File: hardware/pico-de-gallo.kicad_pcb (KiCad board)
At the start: 4 copper layers, 50 x 69.5 mm, 14 parts, among them J1 Conn_02x08_Odd_Even, J2 Conn_01x02, J3 Conn_01x04, J4 Conn_01x05, J5 Conn_01x02, J6 Conn_01x03, J7 Conn_02x05_Odd_Even

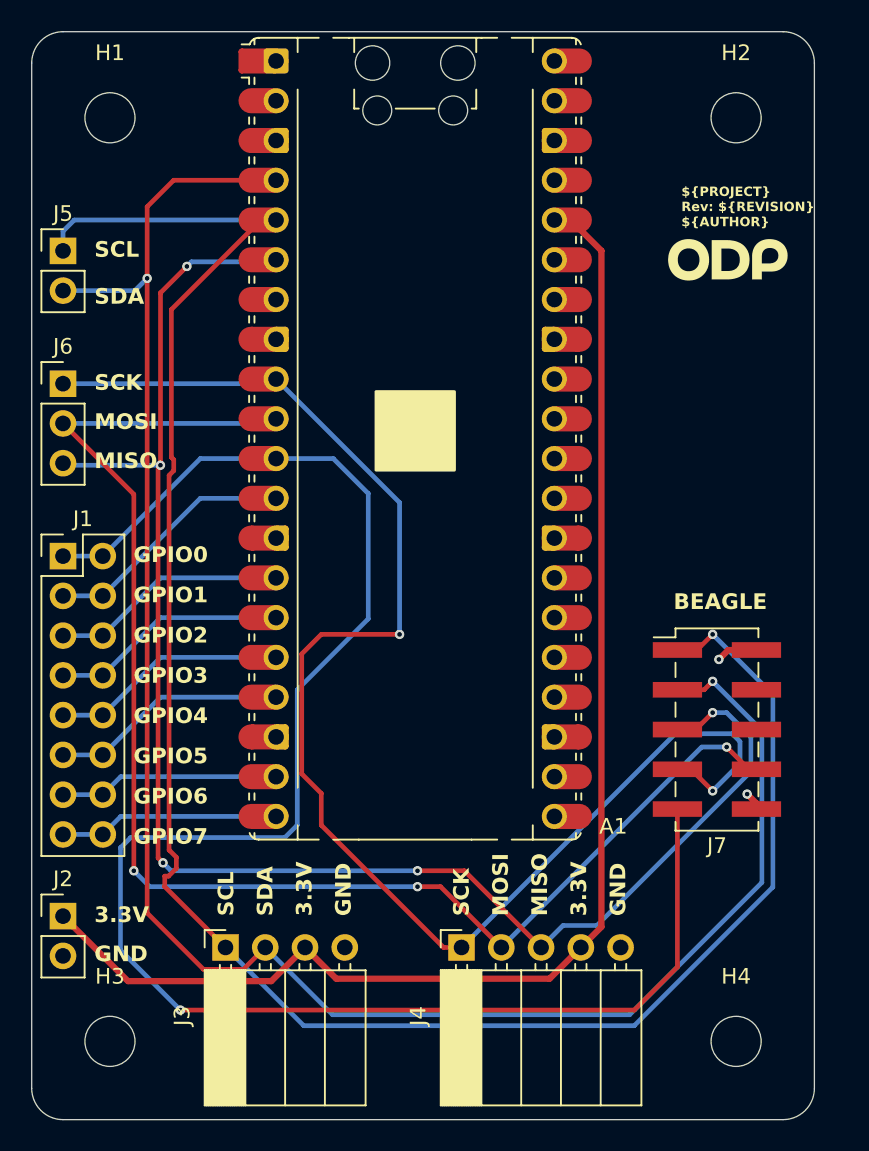
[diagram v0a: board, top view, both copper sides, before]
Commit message: improve 3v3 routing and silkscreen
Signed-off-by: Felipe Balbi <febalbi@microsoft.com>
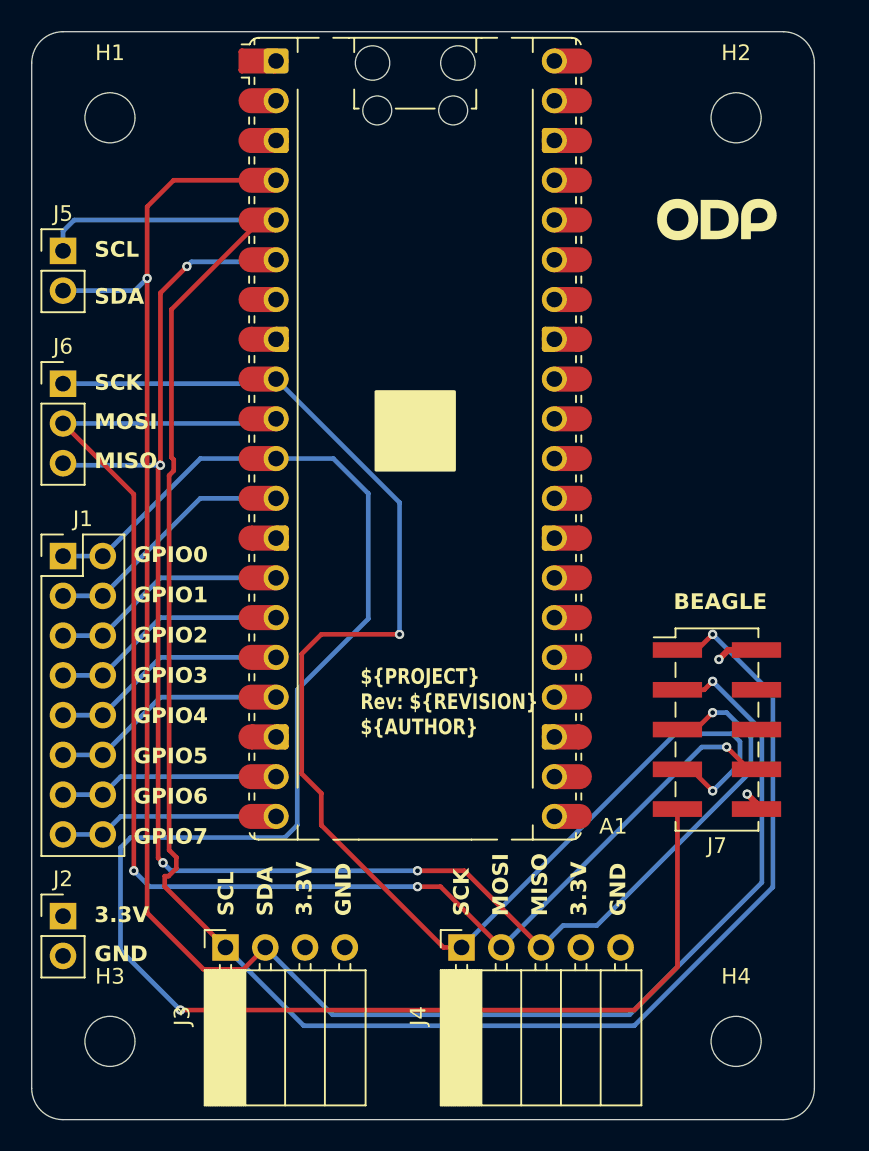
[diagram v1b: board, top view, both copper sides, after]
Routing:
- net +3V3: track 86.2 -> 1.04 mm
